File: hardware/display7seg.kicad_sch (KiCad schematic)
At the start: 23 parts

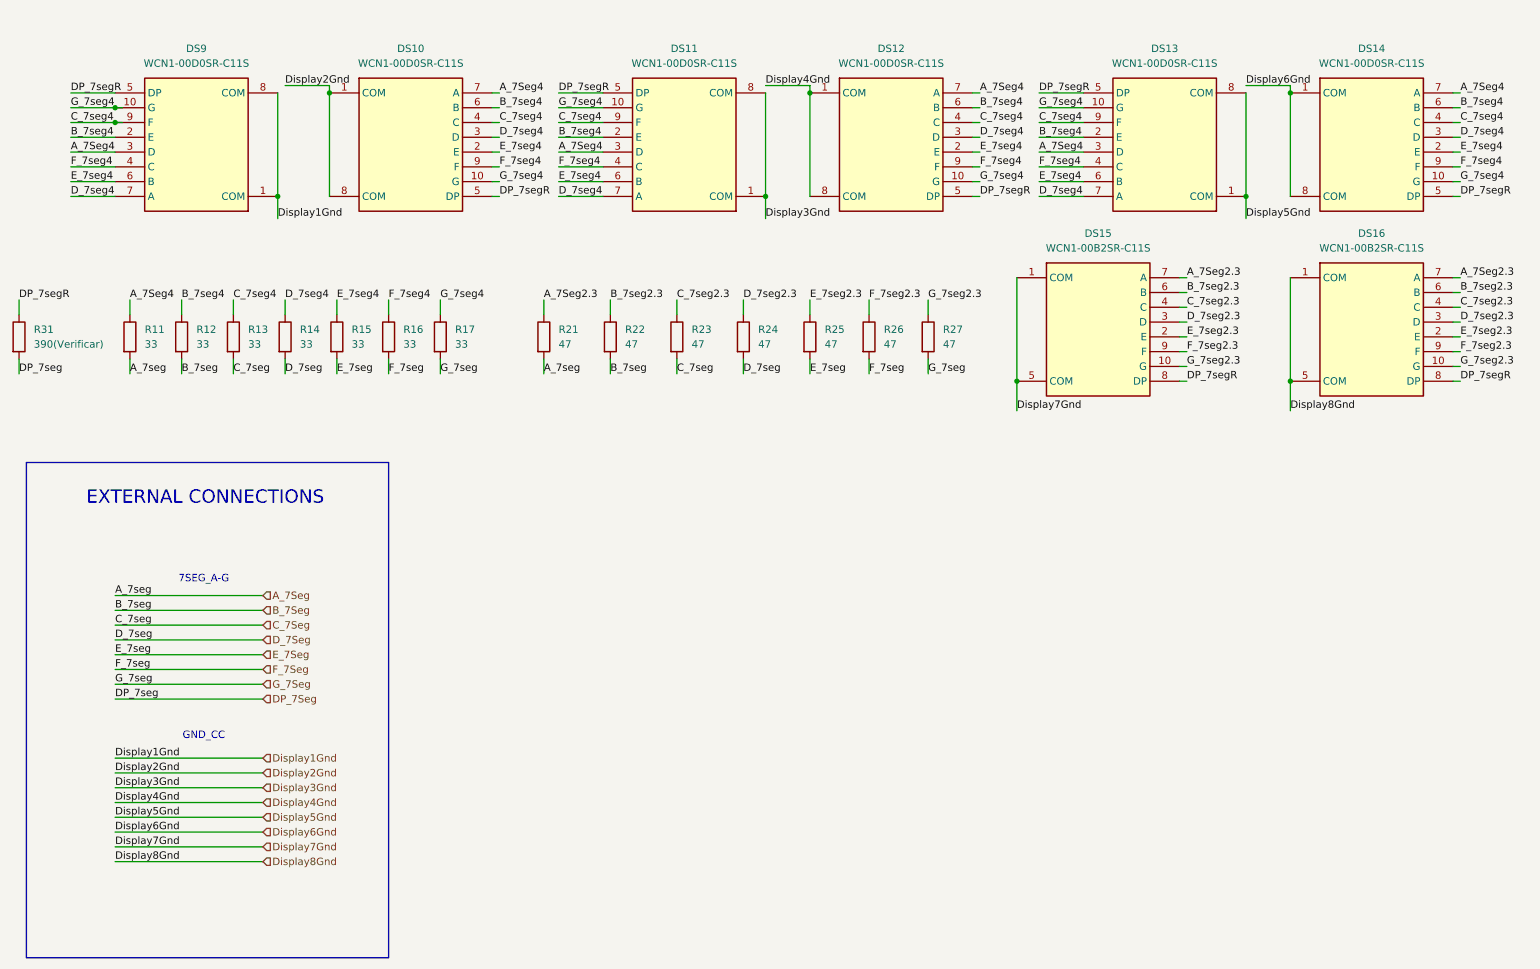
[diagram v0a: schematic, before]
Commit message: Hardware: Rename Temp to RTC-Sensor and Update Schematics
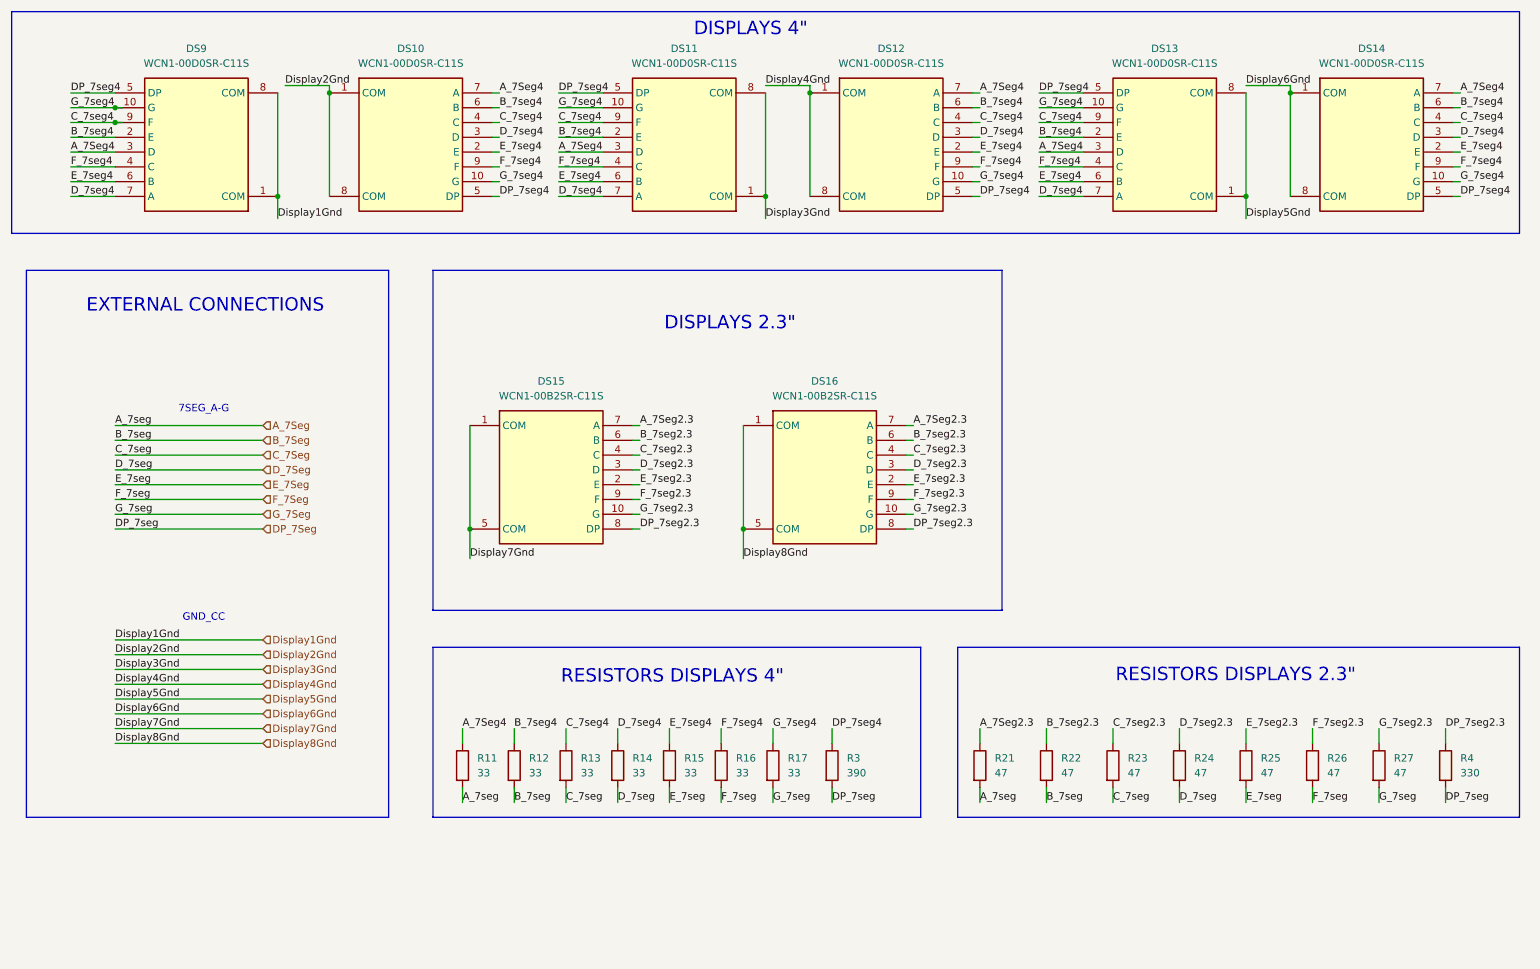
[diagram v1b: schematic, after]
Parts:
- added R4: 330, symbol Device:R
- R3: renamed from R31; value 390(Verificar) -> 390
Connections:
- net DP_7Seg: now also R4.2
- net DP_7segR renamed DP_7seg4
- net DP_7seg4: no longer DS15.8 (DP), DS16.8 (DP)
- new net DP_7seg2.3: DS15.8 (DP), DS16.8 (DP), R4.1
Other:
- note added: "DISPLAYS 2.3""
- note added: "DISPLAYS 4""
- note added: "RESISTORS DISPLAYS 2.3""
- note added: "RESISTORS DISPLAYS 4""
- moved on the sheet: DS15, DS16, R11, R12, R13, R14, R15, R16, R17, R21, R22, R23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
